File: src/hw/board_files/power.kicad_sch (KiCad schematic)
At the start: 15 parts, among them J5 JST??, U1 XC6220B331MR, U7 BQ24074RGT

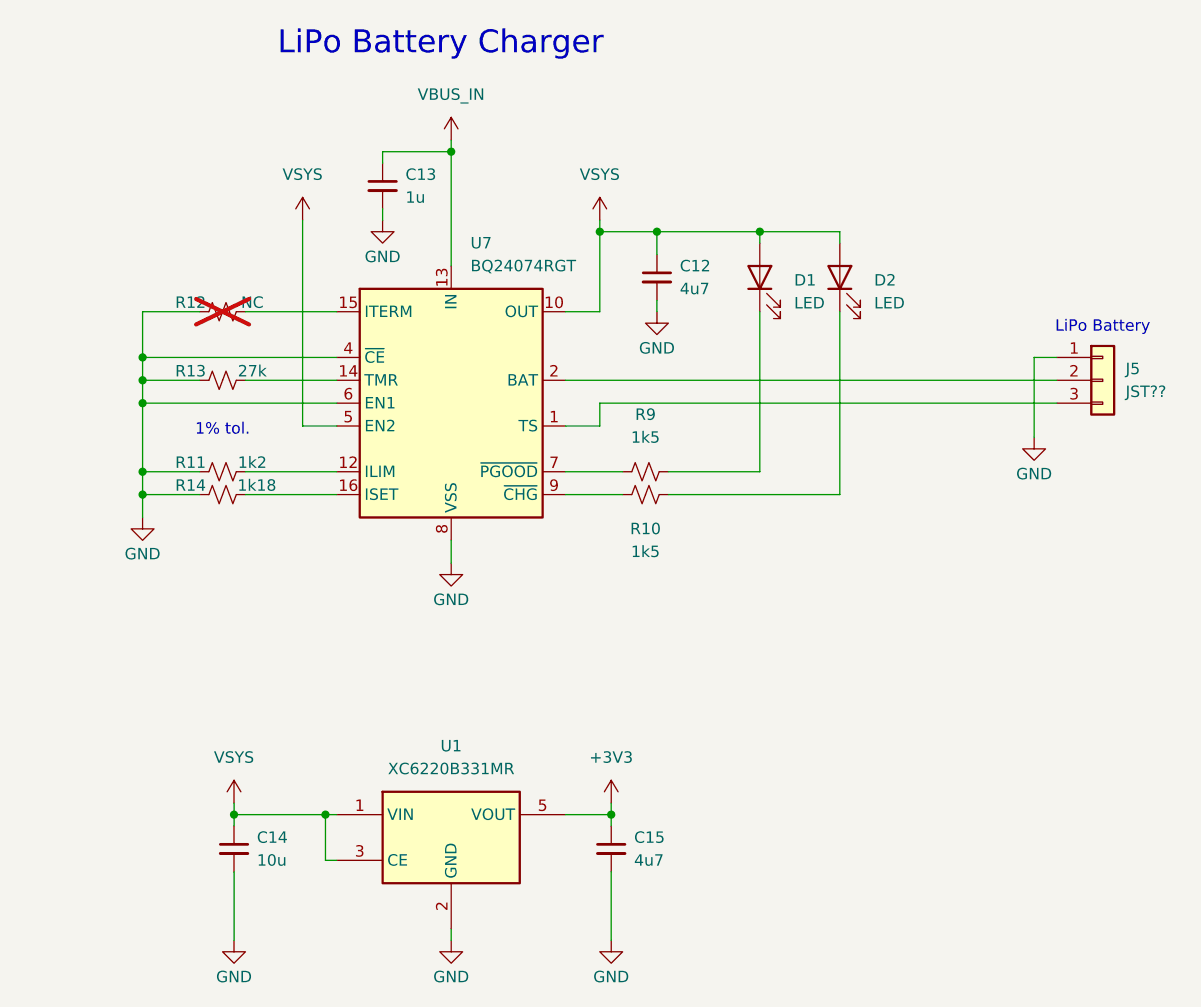
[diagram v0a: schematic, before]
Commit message: Finishing schematic. Need to review and clean up
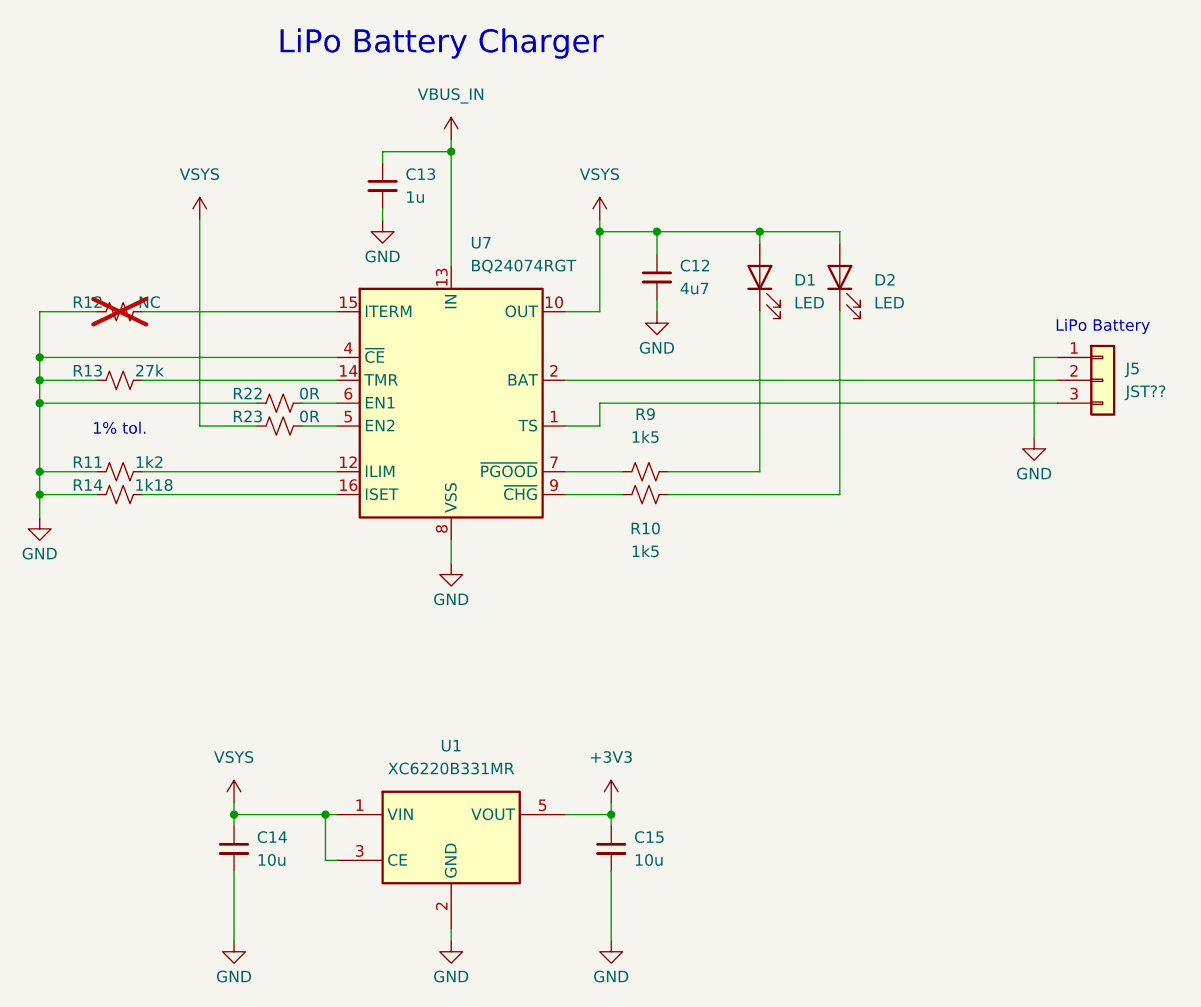
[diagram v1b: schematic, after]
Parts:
- added R22, R23: 0R, symbol Device:R_Small_US
- C15: value 4u7 -> 10u
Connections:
- net GND: now also R22.2; no longer U7.6 (EN1)
- net VSYS: now also R23.2; no longer U7.5 (EN2)
- new net: R22.1, U7.6 (EN1)
- new net: R23.1, U7.5 (EN2)
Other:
- moved on the sheet: R11, R12, R13, R14
